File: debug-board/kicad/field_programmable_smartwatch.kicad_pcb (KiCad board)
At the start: 4 copper layers, 35 x 39 mm, 40 parts, among them IC1 BQ24040DSQR, IC2 STM32WB55CEU6, J1 SPI_Header, J2 LPUART_Header, J3 DX07S016JA1R1500, J4 GPIO_Header, Q1 Q_PMOS_DGS, SW2 SW_DIP_x01, Y1 32M, Y2 32.768k

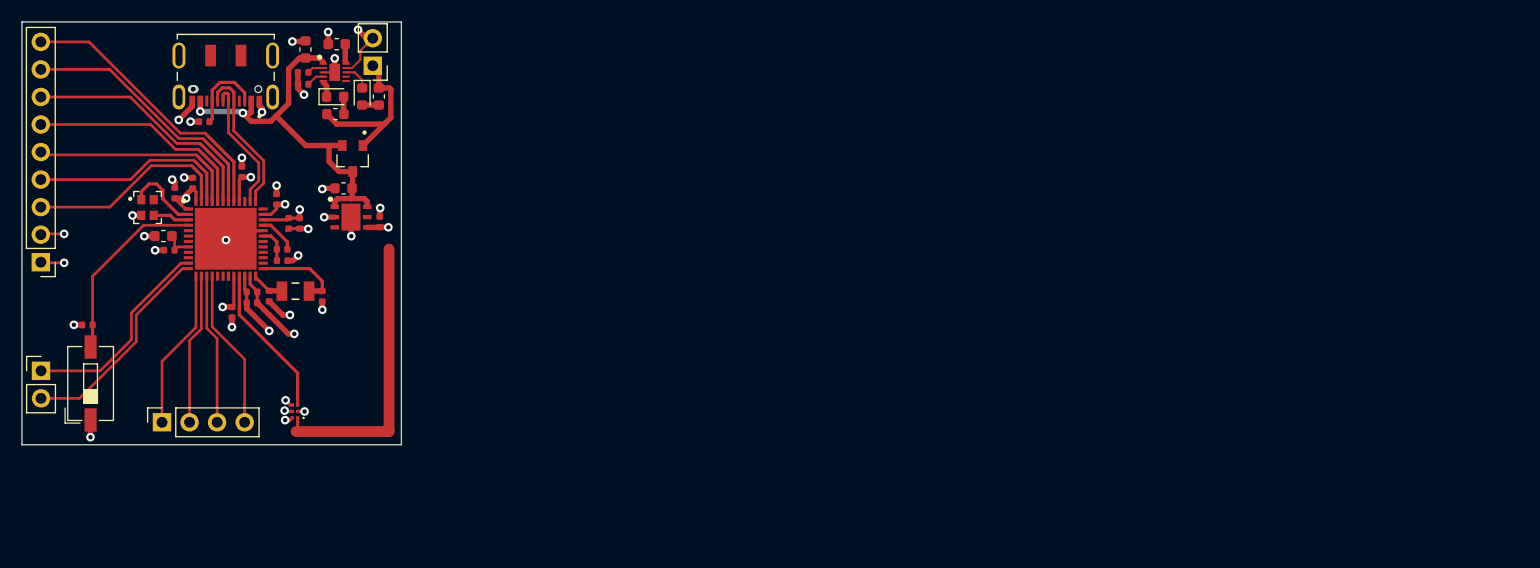
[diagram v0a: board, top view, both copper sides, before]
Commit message: Rework debug board design
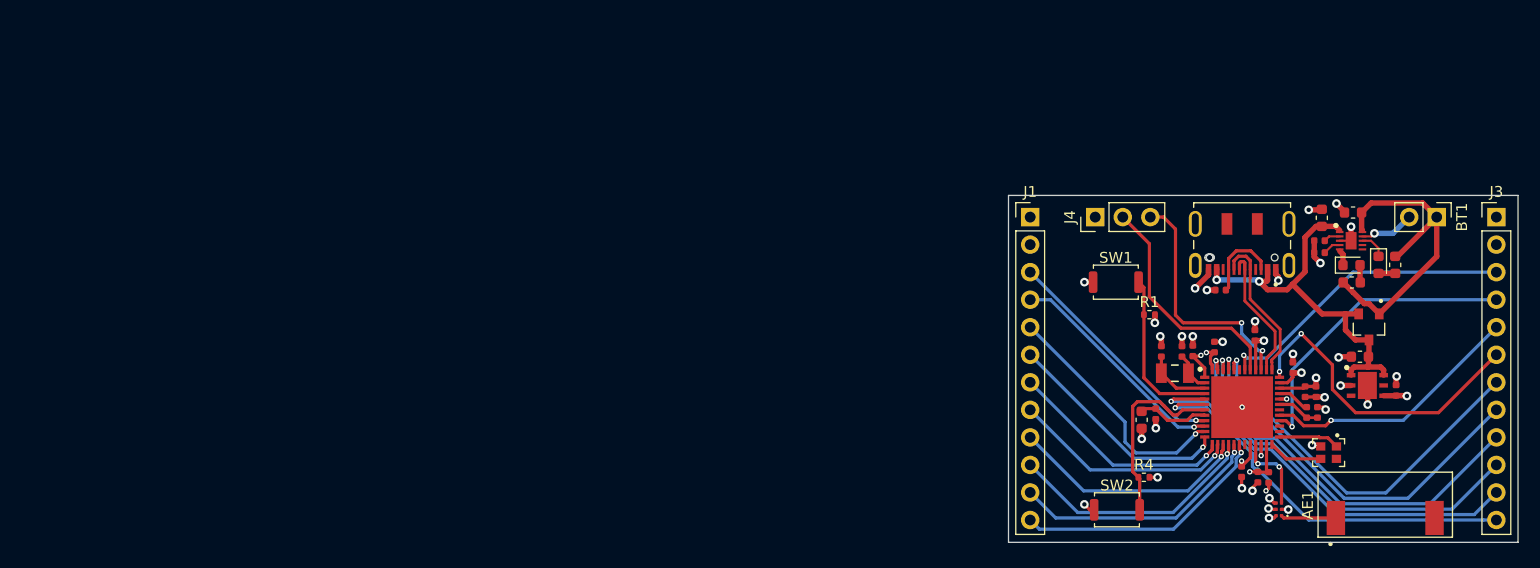
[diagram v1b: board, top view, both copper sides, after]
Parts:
- removed the J2 at (41.8, 83.2)
- removed the R7 at (46.0, 79.0)
- added AE1: Antenna, W3006:W3006, F.Cu at (165.8, 96.8)
- added J3: GPIO Header 2, Connector_PinHeader_2.54mm:PinHeader_1x12_P2.54mm_Vertical, F.Cu at (176.0, 69.0)
- added R1: 100k, Resistor_SMD:R_0402_1005Metric, F.Cu at (144.0, 78.0)
- added R4: 100k, Resistor_SMD:R_0402_1005Metric, F.Cu at (143.5, 93.0)
- added SW1: SW_Push, Button_Switch_SMD:SW_Push_SPST_NO_Alps_SKRK, F.Cu at (140.9, 75.0)
- J1: value SPI_Header -> GPIO Header 1; footprint Connector_PinSocket_2.54mm:PinSocket_1x04_P2.54mm_Vertical -> Connector_PinHeader_2.54mm:PinHeader_1x12_P2.54mm_Vertical
- J4: value GPIO_Header -> SWD Header; footprint Connector_PinHeader_2.54mm:PinHeader_1x09_P2.54mm_Vertical -> Connector_PinHeader_2.54mm:PinHeader_1x03_P2.54mm_Vertical
- SW2: value SW_DIP_x01 -> SW_Push; footprint Button_Switch_SMD:SW_DIP_SPSTx01_Slide_6.7x4.1mm_W6.73mm_P2.54mm_LowProfile_JPin -> Button_Switch_SMD:SW_Push_SPST_NO_Alps_SKRK
- moved Y1 111.3 mm to (160.5, 90.7), turned to 270 degrees
- moved BT1 99.1 mm to (170.5, 69.0), turned to 270 degrees
- moved J4 97.3 mm to (139.0, 69.0), turned to 90 degrees
- moved C14 96.5 mm to (159.5, 87.0), turned to 90 degrees
- moved L1 95.7 mm to (158.5, 87.0), turned to 90 degrees
- moved C11 95.5 mm to (150.0, 81.0)
- moved SW2 95.4 mm to (141.0, 96.0), turned to 0 degrees
- moved C6 95.3 mm to (155.0, 93.0), turned to 270 degrees
- moved C4 95.0 mm to (159.4, 85.1)
- moved C7 95.0 mm to (158.4, 85.1)
- moved IC2 95.0 mm to (152.6, 86.5)
- moved J2 95.0 mm to (152.6, 72.7)
- moved C1 95.0 mm to (159.9, 69.1)
- moved C10 95.0 mm to (162.8, 68.6)
- moved C12 95.0 mm to (163.4, 81.9)
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- renumbered C5 to C10, C9 to C11, C20 to C12, C10 to C13, C11 to C14, C21 to C15, C18 to C17, C6 to C2, C13 to C3, C17 to C4, C7 to C5, C14 to C6, C19 to C7, C12 to C9, J3 to J2, R9 to R2, R1 to R3, R2 to R5, R3 to R6, R6 to R7
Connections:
- net Net-(IC2-Pad19) renamed /PB2
- C16 pad 1: /OSC_IN -> /OSC32k_IN
- C17 pad 1: /OSC_OUT -> /OSC32k_OUT
- IC2 pad 10: Net-(IC2-Pad10) -> /PA1
- IC2 pad 11: /LPUART_TX -> /PA2
- IC2 pad 12: /LPUART_RX -> /PA3
- IC2 pad 13: /NSS -> /PA4
- IC2 pad 14: /SCK -> /PA5
- IC2 pad 15: /MISO -> /PA6
- IC2 pad 16: /MOSI -> /PA7
- IC2 pad 17: Net-(IC2-Pad17) -> /PA8
- IC2 pad 18: Net-(IC2-Pad18) -> /PA9
- IC2 pad 2: /OSC32_IN -> /OSC32k_IN
- IC2 pad 24: /OSC_OUT -> /OSC32M_OUT
- IC2 pad 25: /OSC_IN -> /OSC32M_IN
- IC2 pad 28: Net-(IC2-Pad28) -> /PB0
- IC2 pad 29: Net-(IC2-Pad29) -> /PB1
- IC2 pad 3: /OSC32_OUT -> /OSC32k_OUT
- IC2 pad 36: Net-(IC2-Pad36) -> /PA10
- IC2 pad 39: Net-(IC2-Pad39) -> /PA13
- IC2 pad 5: Net-(IC2-Pad5) -> /PB8
- IC2 pad 6: Net-(IC2-Pad6) -> /PB9
- IC2 pad 7: Net-(IC2-Pad7) -> /RESET
- IC2 pad 9: Net-(IC2-Pad9) -> /PA0
- J1 pad 1: /NSS -> +3V3
- J1 pad 2: /SCK -> GND
- J1 pad 3: /MISO -> /PA0
- J1 pad 4: /MOSI -> /PA1
- J4 pad 1: +3V3 -> GND
- J4 pad 2: GND -> /PA14
- J4 pad 3: /PB7 -> /PA13
- SW2 pad 2: /BOOT0 -> /RESET
- Y1 pad 1: /OSC32_IN -> /OSC32M_IN
- Y1 pad 3: /OSC32_OUT -> /OSC32M_OUT
- Y2 pad 1: /OSC_IN -> /OSC32k_IN
- Y2 pad 2: /OSC_OUT -> /OSC32k_OUT
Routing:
- net /PB8: track 0.00 -> 38.4 mm, vias 0 -> 1
- net /PB9: track 0.00 -> 37.5 mm, vias 0 -> 1
- net /PA10: track 0.00 -> 29.4 mm, vias 0 -> 2
- net /PB0: track 0.00 -> 28.2 mm, vias 0 -> 1
- net /PB1: track 0.00 -> 24.2 mm, vias 0 -> 1
- net /PA9: track 0.00 -> 24.0 mm, vias 0 -> 1
- net /PA8: track 0.00 -> 23.4 mm, vias 0 -> 1
- net /PA7: track 0.00 -> 23.4 mm, vias 0 -> 1
- net /PA2: track 0.00 -> 22.8 mm, vias 0 -> 1
- net /PB3: track 22.7 -> 0.00 mm
- net /PA13: track 0.00 -> 22.5 mm, vias 0 -> 2
- net /PA6: track 0.00 -> 22.2 mm, vias 0 -> 1
- net Net-(AE1-Pad1): track 27.1 -> 5.10 mm
- net /PA0: track 0.00 -> 21.8 mm, vias 0 -> 1
- net /PA3: track 0.00 -> 21.3 mm, vias 0 -> 1
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- added copper zone on In1.Cu, net +3V3
- added copper zone on In2.Cu, net GND
- removed copper zone on In2.Cu, net +3V3
- removed copper zone on In1.Cu, net GND
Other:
- board size 35 x 39 mm -> 47 x 32 mm
- net class Default: clearance 0.2 -> 0.1
- rule trace_clearance: 0.2 -> 0.1
- rule trace_min: 0.2 -> 0.15
- rule via_min_drill: 0.3 -> 0.2

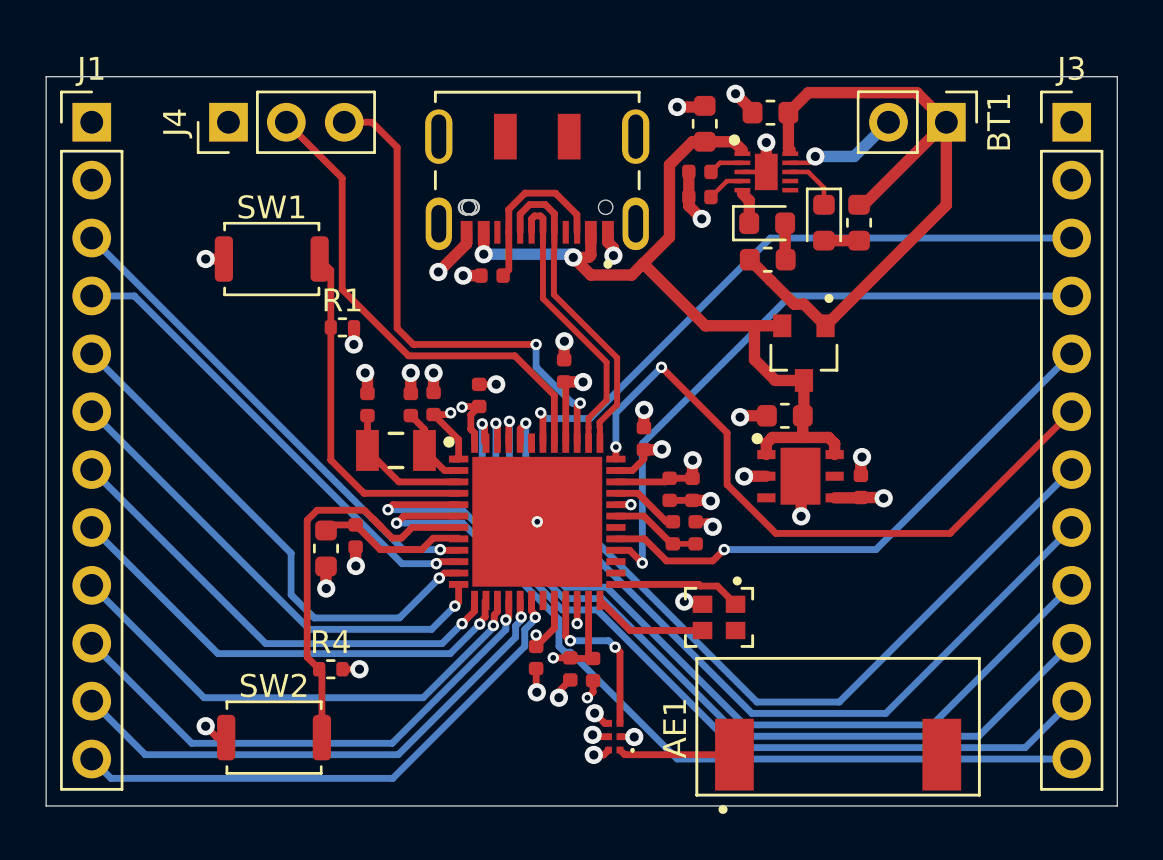
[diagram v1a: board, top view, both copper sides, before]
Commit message: Add labels to PCB components. Remove unneeded files
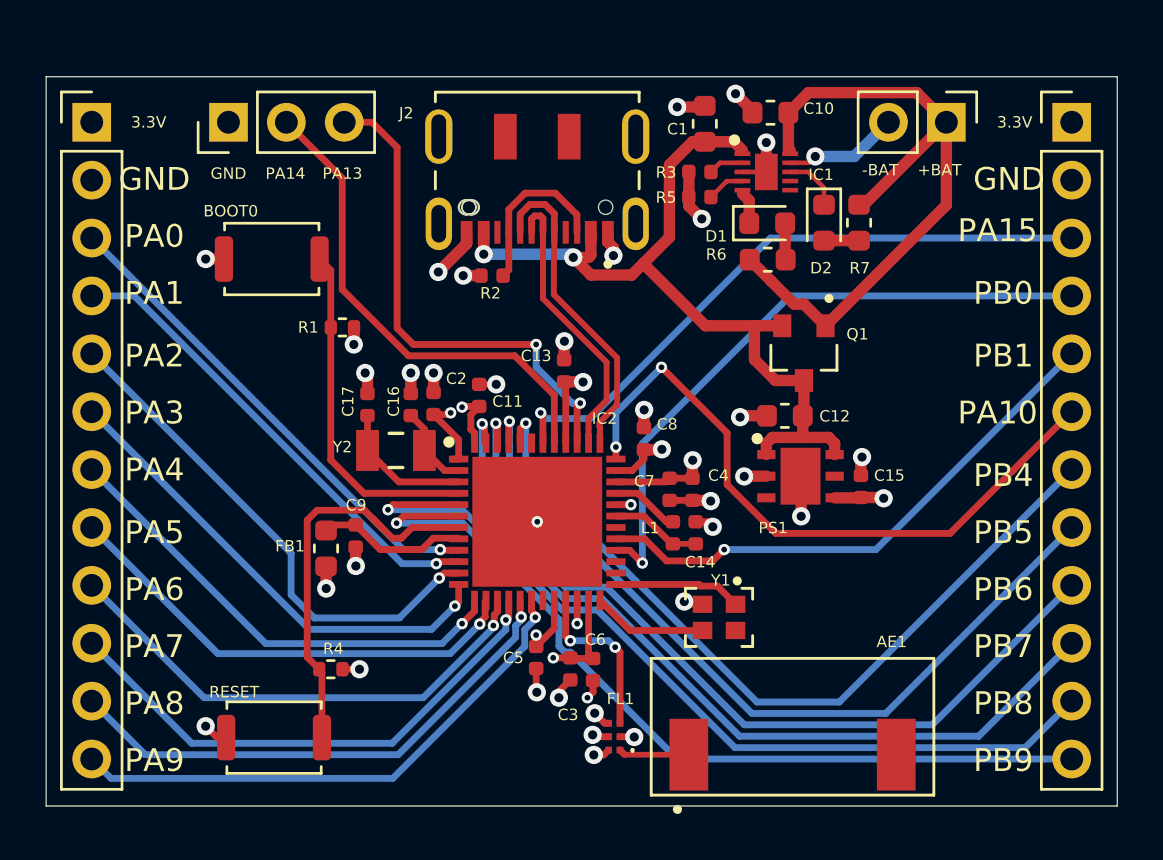
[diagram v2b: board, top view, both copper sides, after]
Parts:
- moved AE1 2.00 mm to (163.8, 96.8)
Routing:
- net Net-(AE1-Pad1): track 5.10 -> 3.10 mm
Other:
- board text added: "+BAT"
- board text added: "-BAT"
- board text added: "3.3V"
- board text added: "AE1"
- board text added: "BOOT0"
- board text added: "C1"
- board text added: "C10"
- board text added: "C11"
- board text added: "C12"
- board text added: "C13"
- board text added: "C14"
- board text added: "C15"
- board text added: "C16"
- board text added: "C17"
- board text added: "C2"
- board text added: "C3"
- board text added: "C4"
- board text added: "C5"
- board text added: "C6"
- board text added: "C7"
- board text added: "C8"
- board text added: "C9"
- board text added: "D1"
- board text added: "D2"
- board text added: "FB1"
- board text added: "FL1"
- board text added: "GND"
- board text added: "IC1"
- board text added: "IC2"
- board text added: "J2"
- board text added: "L1"
- board text added: "PA0"
- board text added: "PA1"
- board text added: "PA10"
- board text added: "PA13"
- board text added: "PA14"
- board text added: "PA15"
- board text added: "PA2"
- board text added: "PA3"
- board text added: "PA4"
- board text added: "PA5"
- board text added: "PA6"
- board text added: "PA7"
- board text added: "PA8"
- board text added: "PA9"
- board text added: "PB0"
- board text added: "PB1"
- board text added: "PB4"
- board text added: "PB5"
- board text added: "PB6"
- board text added: "PB7"
- board text added: "PB8"
- board text added: "PB9"
- board text added: "PS1"
- board text added: "Q1"
- board text added: "R1"
- board text added: "R2"
- board text added: "R3"
- board text added: "R4"
- board text added: "R5"
- board text added: "R6"
- board text added: "R7"
- board text added: "RESET"
- board text added: "Y1"
- board text added: "Y2"

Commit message: Set via on reset button to GND instead of 3.3V
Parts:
- D1: value LED_Small -> LED_Small_Red
- D2: value LED_Small -> LED_Small_Green
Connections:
- R4 pad 2: GND -> +3V3
- SW2 pad 1: +3V3 -> GND

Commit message: Updated debug board
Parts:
- removed BT1: 3.7, Connector_PinHeader_2.54mm:PinHeader_1x02_P2.54mm_Vertical
- removed C1, C10: 1u, Capacitor_SMD:C_0603_1608Metric
- removed D1: LED_Small_Red, Diode_SMD:D_0603_1608Metric
- removed D2: LED_Small_Green, Diode_SMD:D_0603_1608Metric
- removed IC1: BQ24040DSQR, BQ2404DSQR:SON40P200X200X80-11N
- removed Q1: Q_PMOS_DGS, SSM3J325F_LF:SSM3J325F_LF
- removed R1: 100k, Resistor_SMD:R_0402_1005Metric
- removed R3: 2.87k, Resistor_SMD:R_0402_1005Metric
- removed R5: 2k, Resistor_SMD:R_0402_1005Metric
- removed R6, R7: 1.5k, Resistor_SMD:R_0603_1608Metric
- removed SW1: SW_Push, Button_Switch_SMD:SW_Push_SPST_NO_Alps_SKRK
- moved SW2 43.6 mm to (172.1, 65.4), turned to 270 degrees
- moved R4 37.8 mm to (172.6, 68.9)
- moved J1 23.2 mm to (155.7, 64.5)
- moved J4 20.0 mm to (158.4, 73.5)
- moved FL1 15.4 mm to (168.9, 87.6)
- moved FB1 15.3 mm to (158.2, 84.4)
- moved C9 15.3 mm to (159.5, 83.9)
- moved C11 13.3 mm to (162.5, 76.5)
- moved C13 13.3 mm to (166.2, 75.4)
- moved C14 13.3 mm to (172.0, 82.5)
- moved C2 13.3 mm to (160.5, 76.8)
- moved C4 13.3 mm to (171.9, 80.6)
- moved C7 13.3 mm to (170.9, 80.6)
- moved C8 13.3 mm to (169.7, 78.4)
- moved IC2 13.3 mm to (165.1, 82.0)
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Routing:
- net /+BAT: track 30.5 -> 0.00 mm
- net /PA10: track 29.4 -> 8.60 mm, vias 2 -> 1
- net GND: track 39.9 -> 19.9 mm, vias 34 -> 25
- net /VBUS: track 37.2 -> 18.1 mm, vias 2 -> 0
- net /PB8: track 38.4 -> 19.8 mm
- net /PB9: track 37.5 -> 21.6 mm
- net /BOOT0: track 15.2 -> 0.00 mm
- net /PB7: track 36.5 -> 21.3 mm
- net /PB6: track 36.8 -> 22.1 mm
- net /PA14: track 21.7 -> 8.12 mm
- net /PA13: track 22.5 -> 9.08 mm, vias 2 -> 0
- net /RESET: track 17.9 -> 30.7 mm, vias 0 -> 2
- net /PB5: track 35.6 -> 22.8 mm
- net /PA7: track 23.4 -> 10.9 mm
- net /PA8: track 23.4 -> 11.3 mm
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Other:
- board size 47 x 32 mm -> 24.3 x 31.5 mm
- board text removed: "+BAT"
- board text removed: "-BAT"
- board text removed: "BOOT0"
- board text removed: "C1"
- board text removed: "C10"
- board text removed: "D1"
- board text removed: "D2"
- board text removed: "IC1"
- board text removed: "Q1"
- board text removed: "R3"
- board text removed: "R5"
- board text removed: "R6"
- board text removed: "R7"

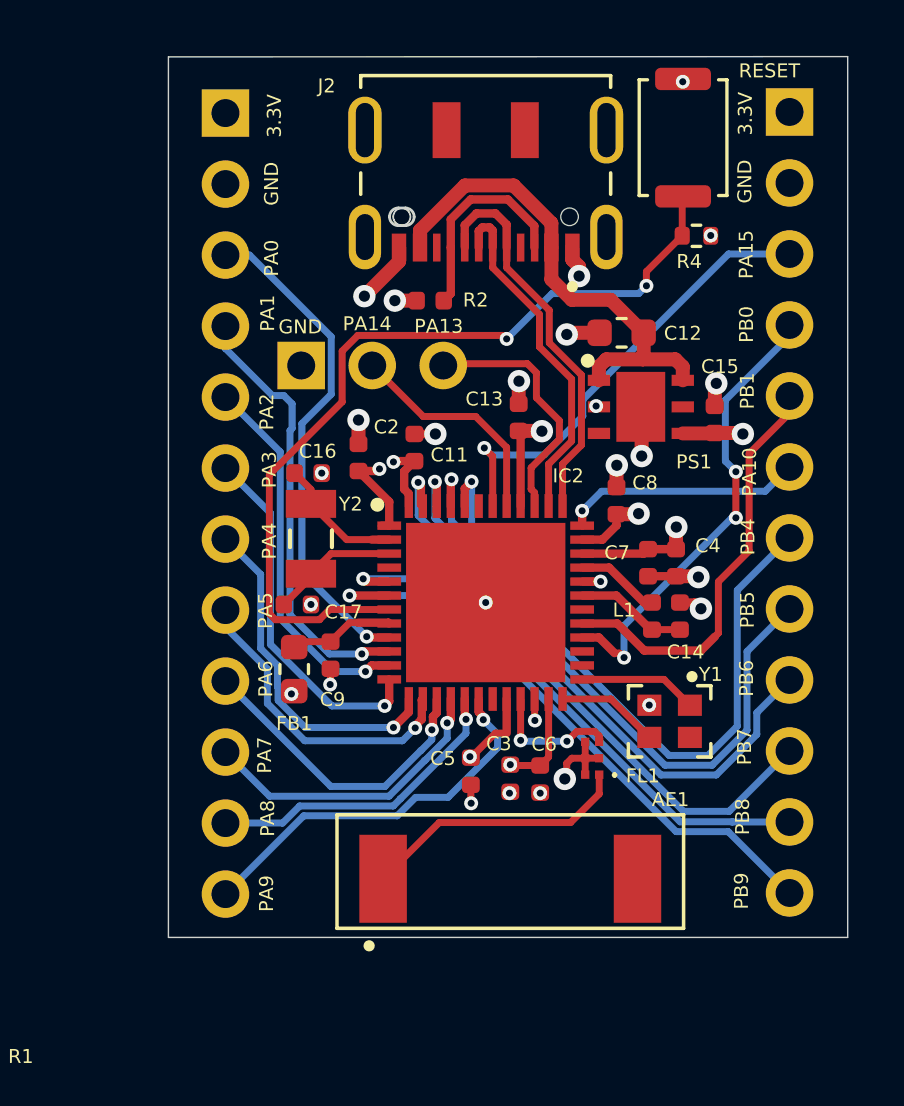
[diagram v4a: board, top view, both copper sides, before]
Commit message: Move the edge cuts in
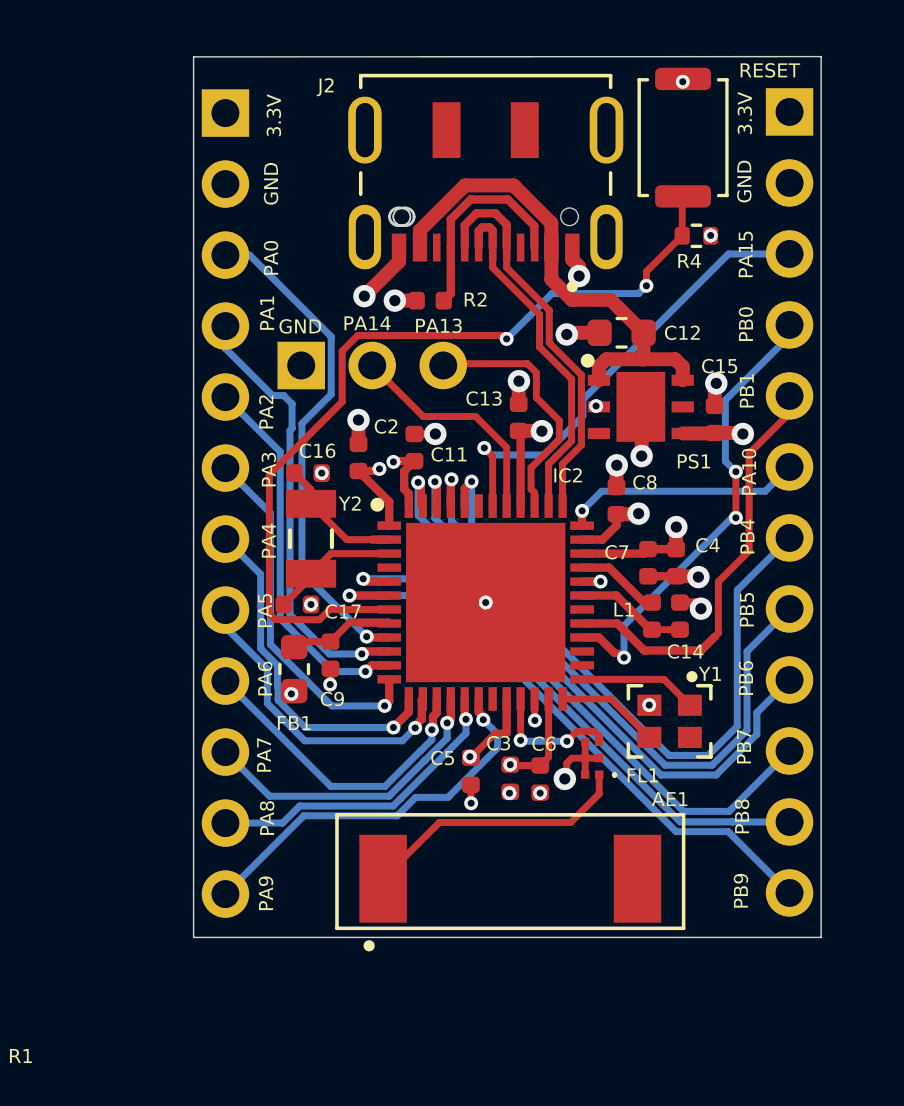
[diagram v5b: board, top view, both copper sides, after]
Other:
- board size 24.3 x 31.5 mm -> 22.5 x 31.5 mm
